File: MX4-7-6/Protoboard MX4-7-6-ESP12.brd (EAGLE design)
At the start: 54.2 x 59.6 mm, 248 parts

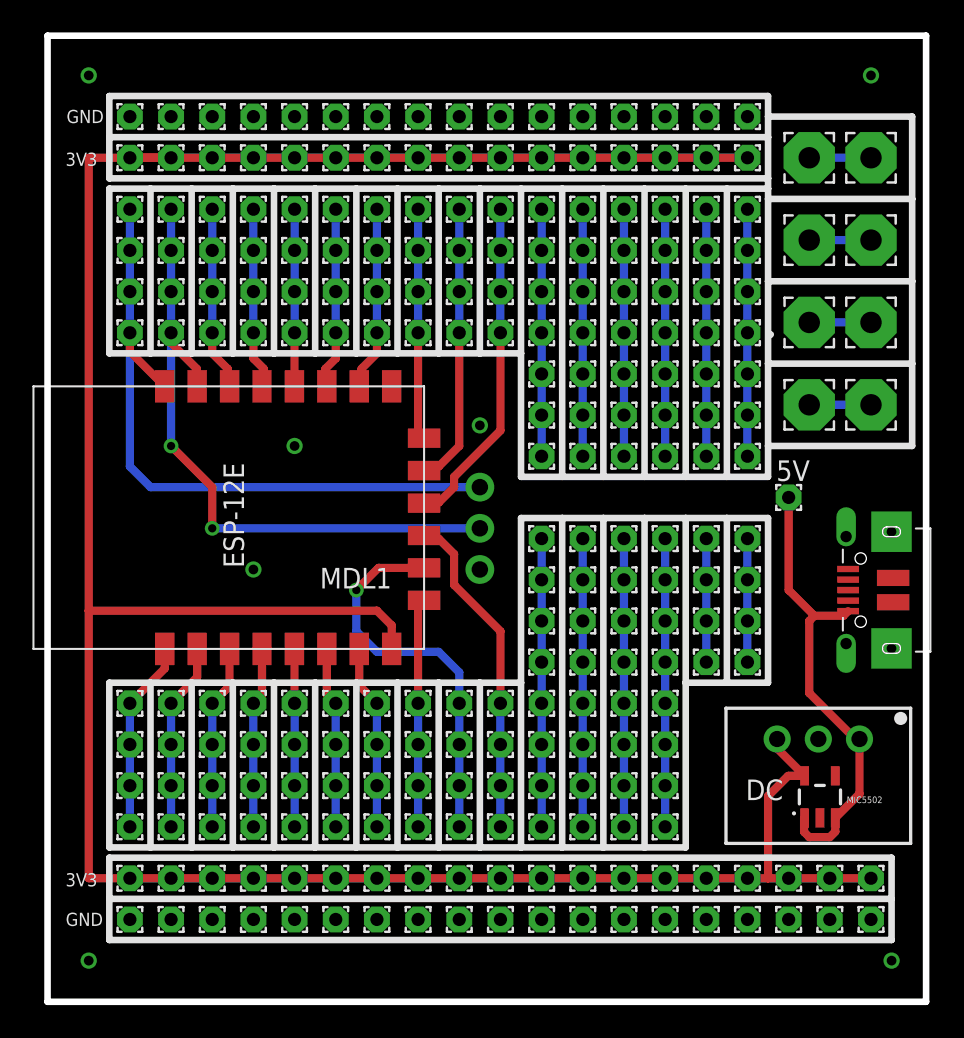
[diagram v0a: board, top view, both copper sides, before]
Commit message: Adjusted Polygon
Adjusted Polygon on all boxes. Changed length on MX-4-7-6 to fit the
box, it was 2mm to long.
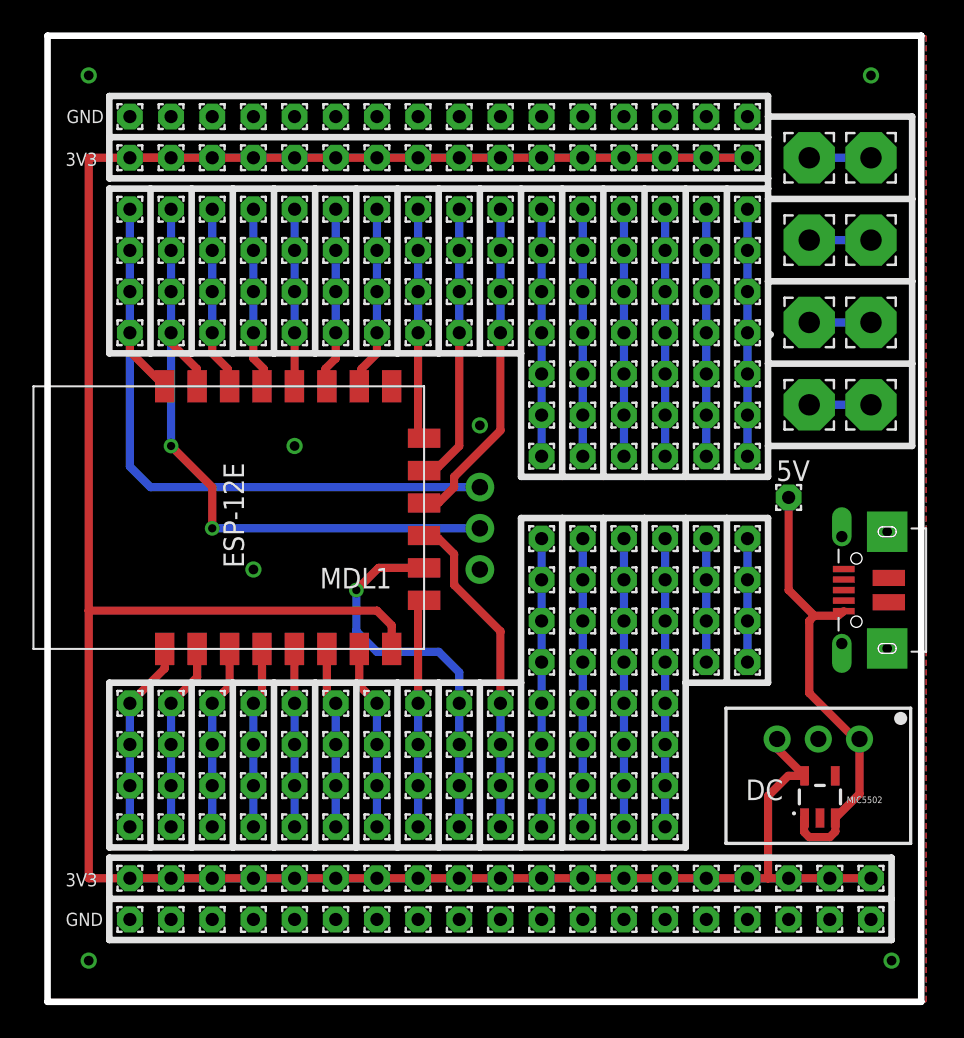
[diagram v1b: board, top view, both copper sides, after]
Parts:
- moved X2 0.27 mm to (49.9, 25.4)
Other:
- board size 54.2 x 59.6 mm -> 53.9 x 59.6 mm
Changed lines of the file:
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@@
 <setting verticaltext="up"/>
 </settings>
-<grid distance="1.27" unitdist="mm" unit="mil" style="dots" multiple="1" display="yes" altdistance="25" altunitdist="mil" altunit="mil"/>
+<grid distance="1.27" unitdist="mm" unit="mm" style="dots" multiple="1" display="yes" altdistance="25" altunitdist="mil" altunit="mm"/>
 <layers>
 <layer number="1" name="Top" color="4" fill="1" visible="yes" active="yes"/>
@@
 <plain>
 <wire x1="0" y1="0" x2="0" y2="59.6" width="0.4064" layer="20"/>
-<wire x1="0" y1="0" x2="54.2" y2="0" width="0.4064" layer="20"/>
-<wire x1="54.2" y1="59.6" x2="0" y2="59.6" width="0.4064" layer="20"/>
-<wire x1="54.2" y1="59.6" x2="54.2" y2="0" width="0.4064" layer="20"/>
+<wire x1="0" y1="0" x2="53.9" y2="0" width="0.4064" layer="20"/>
+<wire x1="53.9" y1="59.6" x2="0" y2="59.6" width="0.4064" layer="20"/>
+<wire x1="53.9" y1="59.6" x2="53.9" y2="0" width="0.4064" layer="20"/>
 <wire x1="44.45" y1="54.61" x2="44.45" y2="53.34" width="0.4064" layer="25"/>
 <wire x1="44.45" y1="53.34" x2="44.45" y2="50.8" width="0.4064" layer="25"/>
@@
 <attribute name="VALUE" x="28.58" y="25.775" size="0.6096" layer="27" rot="R90"/>
 </element>
-<element name="X2" library="microbuilder" package="4UCONN_20329" value="" x="50.165" y="25.4" smashed="yes" rot="R90">
-<attribute name="VALUE" x="56.575" y="22.622" size="0.4064" layer="27" ratio="10" rot="R90"/>
+<element name="X2" library="microbuilder" package="4UCONN_20329" value="" x="49.9" y="25.4" smashed="yes" rot="R90">
+<attribute name="VALUE" x="56.31" y="22.622" size="0.4064" layer="27" ratio="10" rot="R90"/>
 </element>
 <element name="PAD47" library="wirepad" package="1,6/0,8" value="AC" x="7.62" y="18.415" smashed="yes">
@@
 <wire x1="45.72" y1="31.115" x2="45.72" y2="25.4" width="0.508" layer="1"/>
 <wire x1="45.72" y1="25.4" x2="47.3075" y2="23.8125" width="0.508" layer="1"/>
-<wire x1="47.3075" y1="23.8125" x2="49.1025" y2="23.8125" width="0.508" layer="1"/>
-<wire x1="49.1025" y1="23.8125" x2="49.39" y2="24.1" width="0.508" layer="1"/>
 <wire x1="50.0908625" y1="16.211459375" x2="49.828540625" y2="16.211459375" width="0.508" layer="1"/>
 <wire x1="49.828540625" y1="16.211459375" x2="46.99" y2="19.05" width="0.508" layer="1"/>
 <wire x1="46.99" y1="19.05" x2="46.99" y2="23.495" width="0.508" layer="1"/>
 <wire x1="46.99" y1="23.495" x2="47.3075" y2="23.8125" width="0.508" layer="1"/>
+<wire x1="47.3075" y1="23.8125" x2="48.755" y2="23.8125" width="0.508" layer="1"/>
+<wire x1="48.755" y1="23.8125" x2="49.125" y2="24.1" width="0.508" layer="1"/>
 </signal>
 <signal name="VDD">
